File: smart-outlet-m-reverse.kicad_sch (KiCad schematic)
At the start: 11 parts, among them SW1 B3F-3120

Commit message: Renamed things. Removed reference image. Ready for the world.
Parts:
- SW1: symbol merossspecific:SW_SPST_Frame -> designspecific:SW_SPST_Frame
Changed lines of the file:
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@@
 		)
 		(instances
-			(project "Meross smart outlet reverse"
+			(project "smart-outlet-m-reverse"
 				(path "/0b789f5a-74d1-4f81-bd1f-7ac838c6392e"
 					(reference "R8")
@@
 		)
 		(instances
-			(project "Meross smart outlet reverse"
+			(project "smart-outlet-m-reverse"
 				(path "/0b789f5a-74d1-4f81-bd1f-7ac838c6392e"
 					(reference "C14")
@@
 		)
 		(instances
-			(project "Meross smart outlet reverse"
+			(project "smart-outlet-m-reverse"
 				(path "/0b789f5a-74d1-4f81-bd1f-7ac838c6392e"
 					(reference "#PWR014")
@@
 		)
 		(instances
-			(project "Meross smart outlet reverse"
+			(project "smart-outlet-m-reverse"
 				(path "/0b789f5a-74d1-4f81-bd1f-7ac838c6392e"
 					(reference "R23")
@@
 		)
 		(instances
-			(project "Meross smart outlet reverse"
+			(project "smart-outlet-m-reverse"
 				(path "/0b789f5a-74d1-4f81-bd1f-7ac838c6392e"
 					(reference "#PWR017")
@@
 		)
 		(instances
-			(project "Meross smart outlet reverse"
+			(project "smart-outlet-m-reverse"
 				(path "/0b789f5a-74d1-4f81-bd1f-7ac838c6392e"
 					(reference "LED1")
@@
 		)
 		(instances
-			(project "Meross smart outlet reverse"
+			(project "smart-outlet-m-reverse"
 				(path "/0b789f5a-74d1-4f81-bd1f-7ac838c6392e"
 					(reference "R21")
@@
 		)
 		(instances
-			(project "Meross smart outlet reverse"
+			(project "smart-outlet-m-reverse"
 				(path "/0b789f5a-74d1-4f81-bd1f-7ac838c6392e"
 					(reference "MC1")
@@
 		)
 		(instances
-			(project "Meross smart outlet reverse"
+			(project "smart-outlet-m-reverse"
 				(path "/0b789f5a-74d1-4f81-bd1f-7ac838c6392e"
 					(reference "C13")
@@
 		)
 		(instances
-			(project "Meross smart outlet reverse"
+			(project "smart-outlet-m-reverse"
 				(path "/0b789f5a-74d1-4f81-bd1f-7ac838c6392e"
 					(reference "R7")
@@
 		)
 		(instances
-			(project "Meross smart outlet reverse"
+			(project "smart-outlet-m-reverse"
 				(path "/0b789f5a-74d1-4f81-bd1f-7ac838c6392e"
 					(reference "#PWR025")
@@
 	)
 	(symbol
-		(lib_id "merossspecific:SW_SPST_Frame")
+		(lib_id "designspecific:SW_SPST_Frame")
 		(at 90.17 59.69 0)
 		(mirror y)
@@
 		)
 		(instances
-			(project "Meross smart outlet reverse"
+			(project "smart-outlet-m-reverse"
 				(path "/0b789f5a-74d1-4f81-bd1f-7ac838c6392e"
 					(reference "SW1")
@@
 		)
 		(instances
-			(project "Meross smart outlet reverse"
+			(project "smart-outlet-m-reverse"
 				(path "/0b789f5a-74d1-4f81-bd1f-7ac838c6392e"
 					(reference "#PWR03")
@@
 		)
 		(instances
-			(project "Meross smart outlet reverse"
+			(project "smart-outlet-m-reverse"
 				(path "/0b789f5a-74d1-4f81-bd1f-7ac838c6392e"
 					(reference "#PWR018")
@@
 		)
 		(instances
-			(project "Meross smart outlet reverse"
+			(project "smart-outlet-m-reverse"
 				(path "/0b789f5a-74d1-4f81-bd1f-7ac838c6392e"
 					(reference "NTC1")
@@
 		)
 		(instances
-			(project "Meross smart outlet reverse"
+			(project "smart-outlet-m-reverse"
 				(path "/0b789f5a-74d1-4f81-bd1f-7ac838c6392e"
 					(reference "#PWR016")
@@
 		)
 		(instances
-			(project "Meross smart outlet reverse"
+			(project "smart-outlet-m-reverse"
 				(path "/0b789f5a-74d1-4f81-bd1f-7ac838c6392e"
 					(reference "#PWR020")
@@
 		)
 		(instances
-			(project "Meross smart outlet reverse"
+			(project "smart-outlet-m-reverse"
 				(path "/0b789f5a-74d1-4f81-bd1f-7ac838c6392e"
 					(reference "#PWR024")
@@
 		)
 		(instances
-			(project "Meross smart outlet reverse"
+			(project "smart-outlet-m-reverse"
 				(path "/0b789f5a-74d1-4f81-bd1f-7ac838c6392e"
 					(reference "#PWR015")
@@
 		)
 		(instances
-			(project "Meross smart outlet reverse"
+			(project "smart-outlet-m-reverse"
 				(path "/0b789f5a-74d1-4f81-bd1f-7ac838c6392e"
 					(reference "R19")
@@
 		)
 		(instances
-			(project "Meross smart outlet reverse"
+			(project "smart-outlet-m-reverse"
 				(path "/0b789f5a-74d1-4f81-bd1f-7ac838c6392e"
 					(page "2")
@@
 		)
 		(instances
-			(project "Meross smart outlet reverse"
+			(project "smart-outlet-m-reverse"
 				(path "/0b789f5a-74d1-4f81-bd1f-7ac838c6392e"
 					(page "4")
@@
 		)
 		(instances
-			(project "Meross smart outlet reverse"
+			(project "smart-outlet-m-reverse"
 				(path "/0b789f5a-74d1-4f81-bd1f-7ac838c6392e"
 					(page "3")

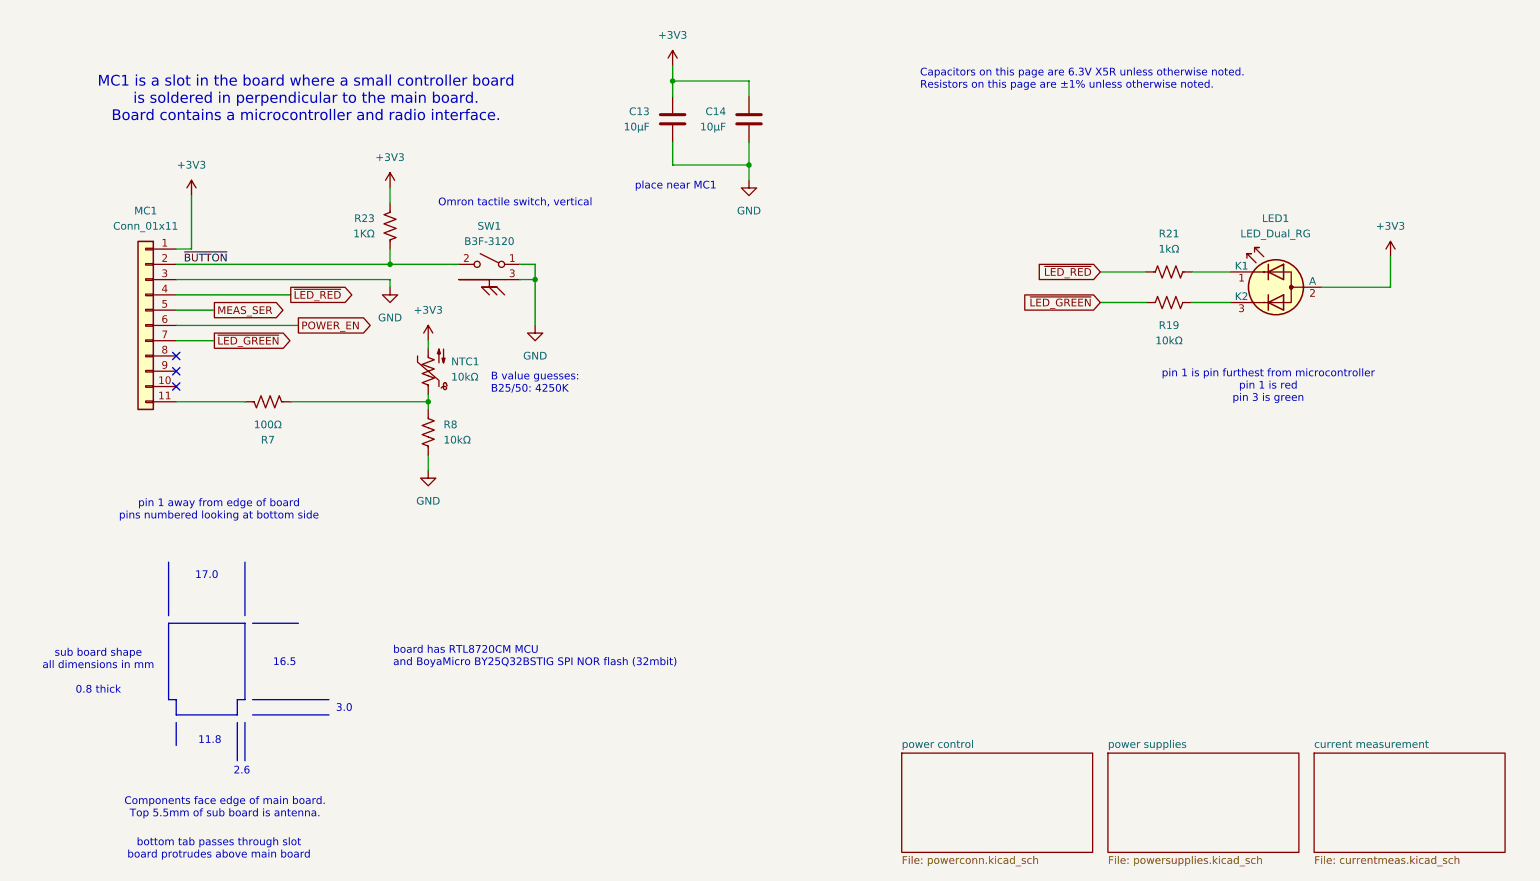
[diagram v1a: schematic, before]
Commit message: Rearranged SMPS circuit. Added a lot of schematic comments. Moved RECT_AC line away from NEUTRAL_SRC (not enough). Updated README greatly. Added pictures. Added PDF schematic.
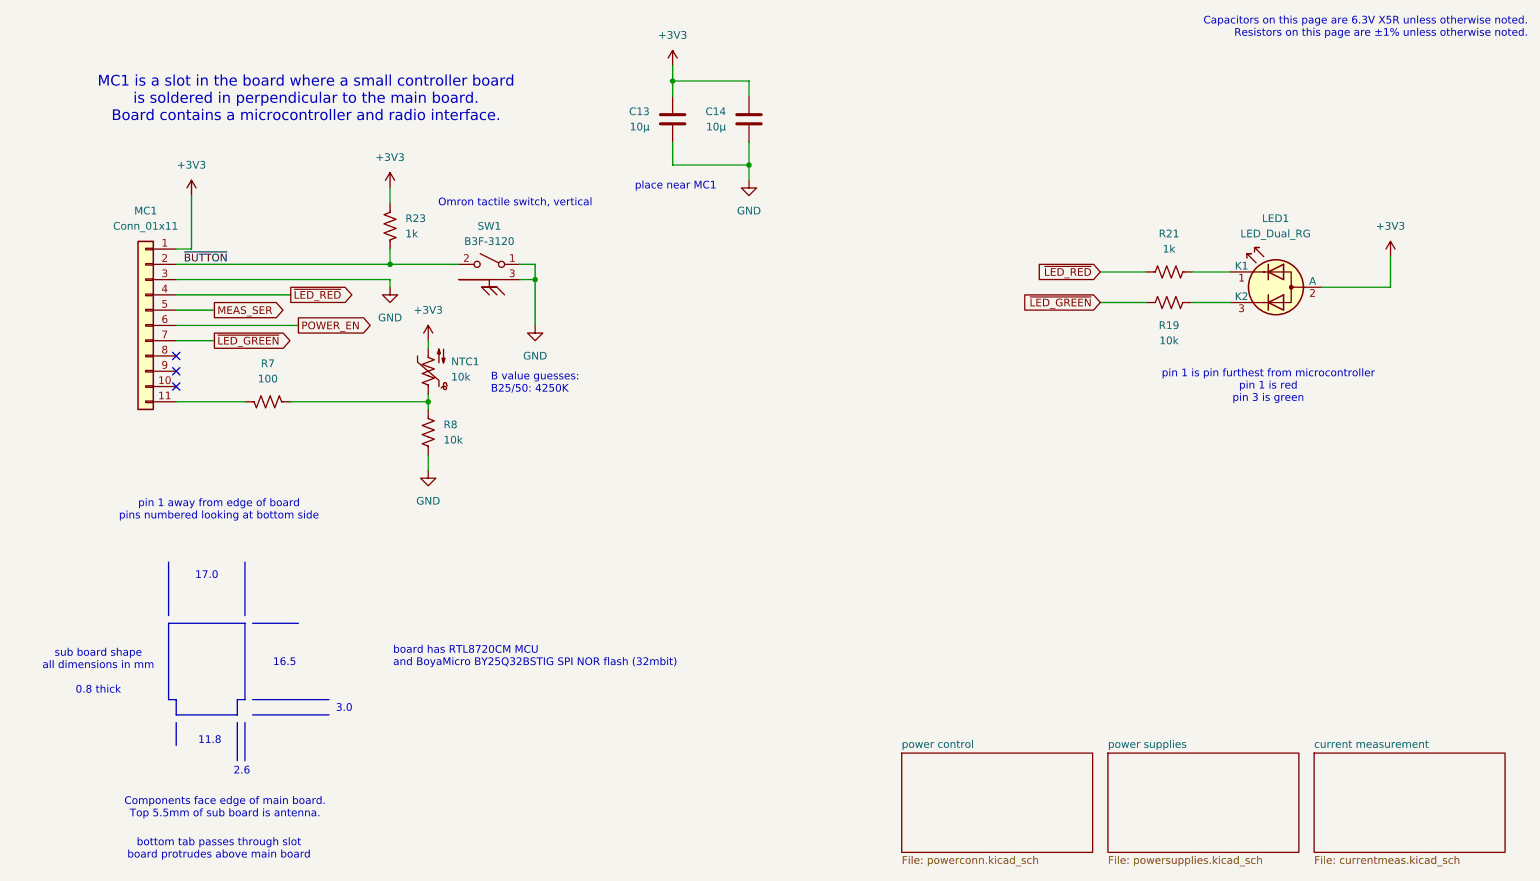
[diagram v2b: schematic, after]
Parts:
- C13, C14: value 10µF -> 10µ
- NTC1, R19, R8: value 10kΩ -> 10k
- R21: value 1kΩ -> 1k
- R23: value 1KΩ -> 1k
- R7: value 100Ω -> 100
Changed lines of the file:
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@@
 	(title_block
 		(title "sensing and controlling interface")
-		(date "2025-07-28")
+		(date "2025-08-17")
+		(rev "a")
 	)
 	(text "2.6"
@@
 	(text "Capacitors on this page are 6.3V X5R unless otherwise noted.\nResistors on this page are ±1% unless otherwise noted."
 		(exclude_from_sim no)
-		(at 161.798 28.956 0)
-		(effects
-			(font
-				(size 1.27 1.27)
-			)
-			(justify left)
+		(at 262.89 20.32 0)
+		(effects
+			(font
+				(size 1.27 1.27)
+			)
+			(justify right)
 		)
 	)
@@
 			)
 		)
-		(property "Value" "10kΩ"
+		(property "Value" "10k"
 			(at 82.55 88.8999 0)
 			(effects
@@
 			)
 		)
-		(property "Value" "10µF"
+		(property "Value" "10µ"
 			(at 129.54 36.8299 0)
 			(effects
@@
 		(fields_autoplaced yes)
 		(property "Reference" "R23"
-			(at 71.12 52.0699 0)
-			(effects
-				(font
-					(size 1.27 1.27)
-				)
-				(justify left)
-			)
-		)
-		(property "Value" "1KΩ"
-			(at 71.12 54.6099 0)
-			(effects
-				(font
-					(size 1.27 1.27)
-				)
-				(justify left)
+			(at 76.2 52.0699 0)
+			(effects
+				(font
+					(size 1.27 1.27)
+				)
+				(justify right)
+			)
+		)
+		(property "Value" "1k"
+			(at 76.2 54.6099 0)
+			(effects
+				(font
+					(size 1.27 1.27)
+				)
+				(justify right)
 			)
 		)
@@
 			)
 		)
-		(property "Value" "1kΩ"
+		(property "Value" "1k"
 			(at 203.2 57.15 90)
 			(effects
@@
 			)
 		)
-		(property "Value" "10µF"
+		(property "Value" "10µ"
 			(at 116.84 36.8299 0)
 			(effects
@@
 		(fields_autoplaced yes)
 		(property "Reference" "R7"
-			(at 53.34 88.9 90)
-			(effects
-				(font
-					(size 1.27 1.27)
-				)
-			)
-		)
-		(property "Value" "100Ω"
-			(at 53.34 86.36 90)
+			(at 53.34 76.2 90)
+			(effects
+				(font
+					(size 1.27 1.27)
+				)
+			)
+		)
+		(property "Value" "100"
+			(at 53.34 78.74 90)
 			(effects
 				(font
@@
 			)
 		)
-		(property "Value" "10kΩ"
+		(property "Value" "10k"
 			(at 83.82 78.4224 0)
 			(effects
@@
 			)
 		)
-		(property "Value" "10kΩ"
+		(property "Value" "10k"
 			(at 203.2 72.39 90)
 			(effects
